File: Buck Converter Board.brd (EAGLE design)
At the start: 120.6 x 47.7 mm, 8 parts, among them J1 POWERPOLE_POWER25A_HORIZONTAL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, J2 POWERPOLE_POWER25A_HORIZONTAL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, J3 POWERPOLE_POWER25A_HORIZONTAL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

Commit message: final updates
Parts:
- D2: value 15KEXX -> (none); device diode:CB429-17 -> diode:DO34Z7
- moved C2 4.57 mm to (29.0, 32.2)
- moved J3 0.10 mm to (104.1, 11.0)
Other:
- board text added: "SEM 2019"
- board text removed: "SEM 2018"
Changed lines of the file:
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@@
 <rectangle x1="71.695" y1="44.405" x2="71.975" y2="44.415" layer="25"/>
 <text x="50.55" y="36.9" size="0.02" layer="25" font="vector">/Users/louissmidt/Downloads/Untitled-1.BMP</text>
-<text x="65.63" y="0.87" size="1.778" layer="25" font="vector">SEM 2018</text>
+<text x="65.63" y="0.87" size="1.778" layer="25" font="vector">SEM 2019</text>
 </plain>
 <attributes>
@@
 </element>
 <element name="J1" library="powerpoles" package="POWERPOLE_PAIR_25A_HORIZ_G2" value="POWERPOLE_POWER25A_HORIZONTAL_G2" x="13.74625" y="21.75125" smashed="yes" rot="R90"/>
-<element name="J2" library="powerpoles" package="POWERPOLE_PAIR_25A_HORIZ_G2" value="POWERPOLE_POWER25A_HORIZONTAL_G2" x="104.07625" y="33.63" smashed="yes"/>
-<element name="C2" library="rcl" library_urn="urn:adsk.eagle:library:334" package="C0805" package3d_urn="urn:adsk.eagle:package:23617/2" value="" x="24.41625" y="32.54375" smashed="yes" rot="R270">
-<attribute name="NAME" x="25.68625" y="33.81375" size="1.27" layer="25" rot="R270"/>
-<attribute name="SPICEPREFIX" value="C" x="24.41625" y="32.54375" size="1.778" layer="27" rot="R270" display="off"/>
-<attribute name="VALUE" x="21.87625" y="33.81375" size="1.27" layer="27" rot="R270"/>
-</element>
-<element name="J3" library="powerpoles" package="POWERPOLE_PAIR_25A_HORIZ_G2" value="POWERPOLE_POWER25A_HORIZONTAL_G2" x="104.01375" y="10.97625" smashed="yes" rot="R180"/>
+<element name="J2" library="powerpoles" package="POWERPOLE_PAIR_25A_HORIZ_G2" value="POWERPOLE_POWER25A_HORIZONTAL_G2" x="104.11" y="33.63" smashed="yes"/>
+<element name="C2" library="rcl" library_urn="urn:adsk.eagle:library:334" package="C0805" package3d_urn="urn:adsk.eagle:package:23617/2" value="" x="28.96625" y="32.15375" smashed="yes" rot="R270">
+<attribute name="NAME" x="30.23625" y="33.42375" size="1.27" layer="25" rot="R270"/>
+<attribute name="SPICEPREFIX" value="C" x="28.96625" y="32.15375" size="1.778" layer="27" rot="R270" display="off"/>
+<attribute name="VALUE" x="26.42625" y="33.42375" size="1.27" layer="27" rot="R270"/>
+</element>
+<element name="J3" library="powerpoles" package="POWERPOLE_PAIR_25A_HORIZ_G2" value="POWERPOLE_POWER25A_HORIZONTAL_G2" x="104.11" y="10.97625" smashed="yes" rot="R180"/>
 <element name="UEE150W" library="REV Aux Circuit" package="DOSA1/8" value="UEE150W" x="34.57" y="11.42" smashed="yes"/>
-<element name="D2" library="diode" library_urn="urn:adsk.eagle:library:210" package="CB429-17" package3d_urn="urn:adsk.eagle:package:43360/1" value="15KEXX" x="114.29" y="22.845" smashed="yes" rot="R270">
+<element name="D2" library="diode" library_urn="urn:adsk.eagle:library:210" package="DO34Z7" package3d_urn="urn:adsk.eagle:package:43364/1" value="" x="114.29" y="22.845" smashed="yes" rot="R270">
 <attribute name="NAME" x="117.211" y="27.925" size="1.27" layer="25" ratio="10" rot="R270"/>
 </element>
@@
 <vertex x="40.92" y="8.88" curve="90"/>
 <vertex x="50.42375" y="18.38375" curve="90"/>
-<vertex x="38.95125" y="29.85625"/>
-<vertex x="22.95" y="29.85625"/>
-<vertex x="14.74625" y="29.85625" curve="90"/>
+<vertex x="39.41125" y="29.39625"/>
+<vertex x="23.41" y="29.39625"/>
+<vertex x="14.28625" y="29.39625" curve="90"/>
 <vertex x="4.09" y="19.2"/>
 <vertex x="4.09" y="18.88" curve="90"/>
@@
 <contactref element="UEE150W" pad="V-"/>
 <contactref element="UEE150W" pad="ON/OFF"/>
-<wire x1="24.385" y1="31.5625" x2="24.385" y2="28.1275" width="0.6096" layer="1"/>
-<via x="24.38375" y="28.12625" extent="1-16" drill="0.35"/>
-<wire x1="24.385" y1="28.1275" x2="24.38375" y2="28.12625" width="0.6096" layer="1"/>
-<wire x1="24.41625" y1="31.59375" x2="24.385" y2="31.5625" width="0.6096" layer="1"/>
+<via x="29.01375" y="27.62625" extent="1-16" drill="0.35"/>
+<wire x1="28.975" y1="31.195" x2="28.96625" y2="31.20375" width="0.6096" layer="1"/>
+<wire x1="28.975" y1="31.195" x2="28.975" y2="27.665" width="0.6096" layer="1"/>
+<wire x1="29.01375" y1="27.62625" x2="28.975" y2="27.665" width="0.6096" layer="1"/>
 </signal>
 <signal name="V_OUT">

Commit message: changed buck board
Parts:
- removed J1: POWERPOLE_POWER25A_HORIZONTAL_G2, powerpoles:POWERPOLE_PAIR_25A_HORIZ_G2
- added BGND, VBATT: VBATT, master_library:P1-13Y
- added BUCK_GND, BUCK_OUT: TEST_POINTSPAD1-13Y, master_library:P1-13Y
- added U$1: BATTERY, master_library:SB50POWER_CLAW
- D1: value (none) -> 15V
- moved C1 8.82 mm to (104.7, 23.4), turned to 0 degrees
- moved F1 8.79 mm to (23.3, 40.6)
- moved C2 3.95 mm to (29.8, 28.3)
- moved J2 2.62 mm to (104.2, 36.2)
- renumbered D2 to D1
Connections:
- net BGND: now also BGND.TP, U$1.NEG1, U$1.NEG2, U$1.NEG3; no longer J1.BLACK
- net OGND: now also BUCK_GND.TP
- net VBATT: now also U$1.POS1, U$1.POS2, U$1.POS3, VBATT.TP; no longer J1.RED
- net V_OUT: now also BUCK_OUT.TP
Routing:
- net VBATT: track 17.1 -> 0.00 mm
- net V_BATT_FUSED: track 0.00 -> 9.05 mm
- net BGND: track 3.60 -> 4.97 mm
- added copper zone on layer 1, net VBATT
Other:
- board size 120.6 x 47.7 mm -> 146.7 x 51.8 mm

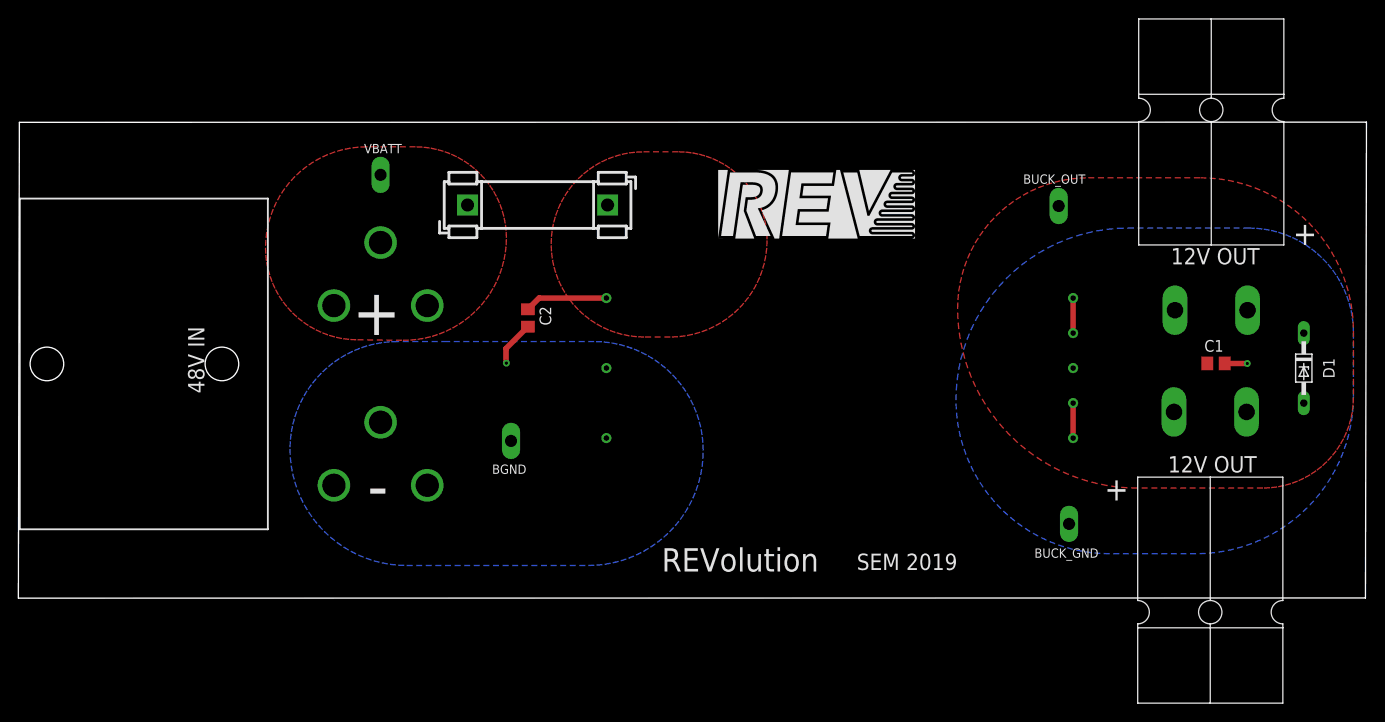
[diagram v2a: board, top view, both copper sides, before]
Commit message: changed boards, added LEDs
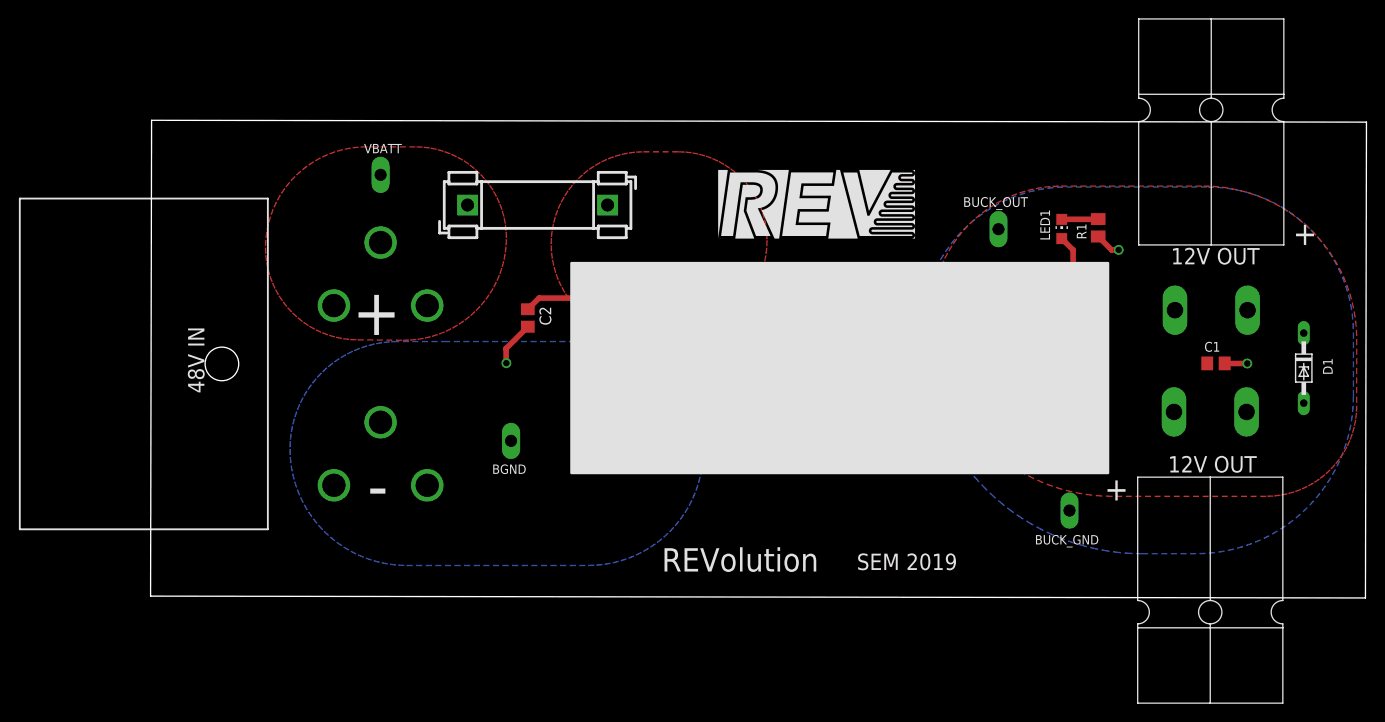
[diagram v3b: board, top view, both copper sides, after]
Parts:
- added LED1: (no value), led:CHIP-LED0805
- added R1: 470, master_library:M0805
- moved BUCK_OUT 7.02 mm to (81.1, 38.0)
- moved BUCK_GND 1.45 mm to (88.8, 7.34)
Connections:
- new net N$1: LED1.C, R1.2
- net OGND: now also R1.1
- net V_OUT: now also LED1.A
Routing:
- net V_OUT: track 3.81 -> 10.8 mm
- net N$1: track 0.00 -> 3.98 mm
- net OGND: track 6.28 -> 9.11 mm, vias 1 -> 2
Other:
- board size 146.7 x 51.8 mm -> 132.3 x 52 mm
- board text added: "Louis Smidt"
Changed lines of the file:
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@@
 <board>
 <plain>
-<wire x1="-25.62625" y1="-2.195" x2="121.00375" y2="-2.175" width="0" layer="20"/>
+<wire x1="-11.23625" y1="-1.975" x2="121.00375" y2="-2.175" width="0" layer="20"/>
 <wire x1="121.00375" y1="-2.175" x2="121.11375" y2="49.61875" width="0" layer="20"/>
-<wire x1="121.11375" y1="49.61875" x2="-25.51625" y2="49.59875" width="0" layer="20"/>
-<wire x1="-25.51625" y1="49.59875" x2="-25.62625" y2="-2.195" width="0" layer="20"/>
+<wire x1="121.11375" y1="49.61875" x2="-11.12625" y2="49.81875" width="0" layer="20"/>
+<wire x1="-11.12625" y1="49.81875" x2="-11.23625" y2="-1.975" width="0" layer="20"/>
 <text x="-7.15375" y="27.37625" size="1.778" layer="25" rot="R270">48V IN</text>
 <text x="109.48375" y="35.915" size="1.778" layer="25" rot="R180">12V OUT</text>
@@
 <text x="50.55" y="36.9" size="0.02" layer="25" font="vector">/Users/louissmidt/Downloads/Untitled-1.BMP</text>
 <text x="65.63" y="0.87" size="1.778" layer="25" font="vector">SEM 2019</text>
+<text x="119.94" y="-1.16" size="1.778" layer="26" rot="MR0">Louis Smidt</text>
 </plain>
 <attributes>
@@
 <elements>
 <element name="C1" library="rcl" library_urn="urn:adsk.eagle:library:334" package="C0805" package3d_urn="urn:adsk.eagle:package:23617/2" value=".47uF" x="104.73" y="23.36" smashed="yes">
-<attribute name="NAME" x="103.46" y="24.63" size="1.27" layer="25"/>
+<attribute name="NAME" x="103.46" y="24.63" size="1.06" layer="25"/>
 <attribute name="SPICEPREFIX" value="C" x="104.73" y="23.36" size="1.778" layer="27" display="off"/>
 </element>
@@
 <element name="UEE150W" library="REV Aux Circuit" package="DOSA1/8" value="UEE150W" x="34.57" y="11.42" smashed="yes"/>
 <element name="D1" library="diode" library_urn="urn:adsk.eagle:library:210" package="DO34Z7" package3d_urn="urn:adsk.eagle:package:43364/1" value="15V" x="114.29" y="22.845" smashed="yes" rot="R270">
-<attribute name="NAME" x="116.381" y="23.935" size="1.27" layer="25" ratio="10" rot="R270"/>
+<attribute name="NAME" x="116.381" y="23.935" size="1.06" layer="25" ratio="10" rot="R270"/>
 </element>
 <element name="U$1" library="master_library" package="SB50POWER_CLAW" package3d_urn="urn:adsk.eagle:package:2274131/1" value="BATTERY" x="-3.47" y="23.3" smashed="yes" rot="R180"/>
@@
 <attribute name="VALUE" x="19.71" y="43.78" size="0.0254" layer="27"/>
 </element>
-<element name="BUCK_OUT" library="master_library" package="P1-13Y" package3d_urn="urn:adsk.eagle:package:2274087/1" value="TEST_POINTSPAD1-13Y" x="87.61" y="40.49" smashed="yes">
-<attribute name="NAME" x="83.7478" y="42.9114" size="1.016" layer="25" ratio="10" rot="SR0"/>
-<attribute name="TP_SIGNAL_NAME" value="" x="86.34" y="36.68" size="1" layer="37"/>
-<attribute name="VALUE" x="87.61" y="40.49" size="0.0254" layer="27"/>
+<element name="BUCK_OUT" library="master_library" package="P1-13Y" package3d_urn="urn:adsk.eagle:package:2274087/1" value="TEST_POINTSPAD1-13Y" x="81.06" y="37.97" smashed="yes">
+<attribute name="NAME" x="77.1978" y="40.3914" size="1.06" layer="25" ratio="10" rot="SR0"/>
+<attribute name="TP_SIGNAL_NAME" value="" x="79.79" y="34.16" size="1" layer="37"/>
+<attribute name="VALUE" x="78.66" y="36.44" size="0.0254" layer="27"/>
 </element>
-<element name="BUCK_GND" library="master_library" package="P1-13Y" package3d_urn="urn:adsk.eagle:package:2274087/1" value="TEST_POINTSPAD1-13Y" x="88.74" y="5.89" smashed="yes">
-<attribute name="NAME" x="84.9678" y="2.2014" size="1.016" layer="25" ratio="10" rot="SR0"/>
-<attribute name="TP_SIGNAL_NAME" value="" x="87.47" y="2.08" size="1" layer="37"/>
-<attribute name="VALUE" x="89.31" y="5.43" size="0.0254" layer="27"/>
+<element name="BUCK_GND" library="master_library" package="P1-13Y" package3d_urn="urn:adsk.eagle:package:2274087/1" value="TEST_POINTSPAD1-13Y" x="88.79" y="7.34" smashed="yes">
+<attribute name="NAME" x="85.0178" y="3.6514" size="1.016" layer="25" ratio="10" rot="SR0"/>
+<attribute name="TP_SIGNAL_NAME" value="" x="87.52" y="3.53" size="1" layer="37"/>
+<attribute name="VALUE" x="89.36" y="6.88" size="0.0254" layer="27"/>
 </element>
 <element name="BGND" library="master_library" package="P1-13Y" package3d_urn="urn:adsk.eagle:package:2274087/1" value="VBATT" x="28" y="14.92" smashed="yes">
@@
 <attribute name="VALUE" x="28" y="14.92" size="0.0254" layer="27"/>
 </element>
+<element name="LED1" library="led" library_urn="urn:adsk.eagle:library:259" package="CHIP-LED0805" package3d_urn="urn:adsk.eagle:package:15818/2" value="" x="87.94" y="37.99" smashed="yes">
+<attribute name="NAME" x="86.67" y="36.72" size="1.06" layer="25" rot="R90"/>
+<attribute name="VALUE" x="90.48" y="36.72" size="1.27" layer="27" rot="R90"/>
+</element>
+<element name="R1" library="master_library" package="M0805" package3d_urn="urn:adsk.eagle:package:2274058/1" value="470" x="91.91" y="38.12" smashed="yes" rot="R90">
+<attribute name="NAME" x="90.64" y="36.85" size="1.06" layer="25" rot="R90"/>
+</element>
 </elements>
 <signals>
@@
 <contactref element="UEE150W" pad="V-"/>
 <contactref element="UEE150W" pad="ON/OFF"/>
-<via x="27.49375" y="23.38625" extent="1-16" drill="0.35"/>
+<via x="27.49375" y="23.38625" extent="1-16" drill="0.69"/>
 <wire x1="29.83625" y1="27.35375" x2="27.455" y2="24.9725" width="0.6096" layer="1"/>
 <wire x1="27.455" y1="24.9725" x2="27.455" y2="23.425" width="0.6096" layer="1"/>
@@
 <contactref element="C1" pad="1"/>
 <polygon width="0.1524" layer="1">
-<vertex x="76.60875" y="29.3325" curve="-90"/>
-<vertex x="90.83625" y="43.56"/>
-<vertex x="103.03625" y="43.56" curve="-90"/>
-<vertex x="119.69375" y="26.9025"/>
-<vertex x="119.69375" y="19.64125" curve="-90"/>
-<vertex x="109.8425" y="9.79"/>
-<vertex x="96.15125" y="9.79" curve="-90"/>
+<vertex x="73.75875" y="28.5325" curve="-90"/>
+<vertex x="87.88625" y="42.66"/>
+<vertex x="103.39625" y="42.66" curve="-90"/>
+<vertex x="120.05375" y="26.0025"/>
+<vertex x="120.05375" y="18.74125" curve="-90"/>
+<vertex x="110.2025" y="8.89"/>
+<vertex x="93.40125" y="8.89" curve="-90"/>
 </polygon>
 <contactref element="D1" pad="C"/>
@@
 <wire x1="89.18" y1="26.66" x2="89.18" y2="30.47" width="0.6096" layer="1"/>
 <contactref element="BUCK_OUT" pad="TP"/>
+<contactref element="LED1" pad="A"/>
+<wire x1="89.18" y1="30.47" x2="89.18" y2="35.7" width="0.6096" layer="1"/>
+<wire x1="89.18" y1="35.7" x2="87.94" y2="36.94" width="0.6096" layer="1"/>
 </signal>
 <signal name="OGND" airwireshidden="yes">
@@
 <contactref element="UEE150W" pad="V_OUT-"/>
 <polygon width="0.1524" layer="16">
-<vertex x="76.431875" y="19.360625" curve="-90"/>
-<vertex x="95.16125" y="38.09"/>
-<vertex x="108.31875" y="38.09" curve="-90"/>
+<vertex x="72.616875" y="26.715625" curve="-90"/>
+<vertex x="88.46125" y="42.56"/>
+<vertex x="103.84875" y="42.56" curve="-90"/>
 <vertex x="119.69375" y="26.715"/>
 <vertex x="119.69375" y="19.76625" curve="-90"/>
 <vertex x="102.5675" y="2.64"/>
-<vertex x="93.1525" y="2.64" curve="-90"/>
+<vertex x="96.6925" y="2.64" curve="-90"/>
 </polygon>
 <contactref element="D1" pad="A"/>
 <wire x1="105.68" y1="23.36" x2="105.69375" y2="23.34625" width="0.6096" layer="1"/>
 <wire x1="105.69375" y1="23.34625" x2="108.14" y2="23.34625" width="0.6096" layer="1"/>
-<via x="108.14" y="23.34625" extent="1-16" drill="0.35"/>
+<via x="108.14" y="23.34625" extent="1-16" drill="0.69"/>
 <contactref element="UEE150W" pad="SNS-"/>
 <wire x1="89.18" y1="19.04" x2="89.18" y2="15.23" width="0.6096" layer="1"/>
 <contactref element="BUCK_GND" pad="TP"/>
+<contactref element="R1" pad="1"/>
+<wire x1="91.91" y1="37.17" x2="93.37" y2="35.71" width="0.6096" layer="1"/>
+<wire x1="93.37" y1="35.71" x2="94.14" y2="35.71" width="0.6096" layer="1"/>
+<via x="94.14" y="35.71" extent="1-16" drill="0.69"/>
+</signal>
+<signal name="N$1">
+<contactref element="LED1" pad="C"/>
+<contactref element="R1" pad="2"/>
+<wire x1="87.94" y1="39.04" x2="91.88" y2="39.04" width="0.6096" layer="1"/>
+<wire x1="91.88" y1="39.04" x2="91.91" y2="39.07" width="0.6096" layer="1"/>
 </signal>
 </signals>
